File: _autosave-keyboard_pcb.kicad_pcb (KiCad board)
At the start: 2 copper layers, 436.2 x 123.8 mm, 214 parts, among them J1 Conn_01x04_Female, J2 , J3 Conn_01x03_Male, SW1 SW_Push, SW10 SW_Push, SW100 SW_Push, SW101 SW_Push, SW102 SW_Push, SW103 SW_Push, SW104 SW_Push, SW105 SW_Push, SW11 SW_Push, SW12 SW_Push, SW13 SW_Push, SW14 SW_Push, SW15 SW_Push, SW16 SW_Push, SW17 SW_Push, SW18 SW_Push, SW19 SW_Push, SW2 SW_Push, SW20 SW_Push, SW21 SW_Push, SW22 SW_Push, SW23 SW_Push, SW24 SW_Push, SW25 SW_Push, SW26 SW_Push, SW27 SW_Push, SW28 SW_Push, SW29 SW_Push, SW3 SW_Push, SW30 SW_Push, SW31 SW_Push, SW32 SW_Push, SW33 SW_Push, SW34 SW_Push, SW35 SW_Push, SW36 SW_Push, SW37 SW_Push, SW38 SW_Push, SW39 SW_Push, SW4 SW_Push, SW40 SW_Push, SW41 SW_Push, SW42 SW_Push, SW43 SW_Push, SW44 SW_Push, SW45 SW_Push, SW46 SW_Push, SW47 SW_Push, SW48 SW_Push, SW49 SW_Push, SW5 SW_Push, SW50 SW_Push, SW51 SW_Push, SW52 SW_Push, SW53 SW_Push, SW54 SW_Push, SW55 SW_Push, SW56 SW_Push, SW57 SW_Push, SW58 SW_Push, SW59 SW_Push, SW6 SW_Push, SW60 SW_Push, SW61 SW_Push, SW62 SW_Push, SW63 SW_Push, SW64 SW_Push, SW65 SW_Push, SW66 SW_Push, SW67 SW_Push, SW68 SW_Push, SW69 SW_Push, SW7 SW_Push, SW70 SW_Push, SW71 SW_Push, SW72 SW_Push, SW73 SW_Push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

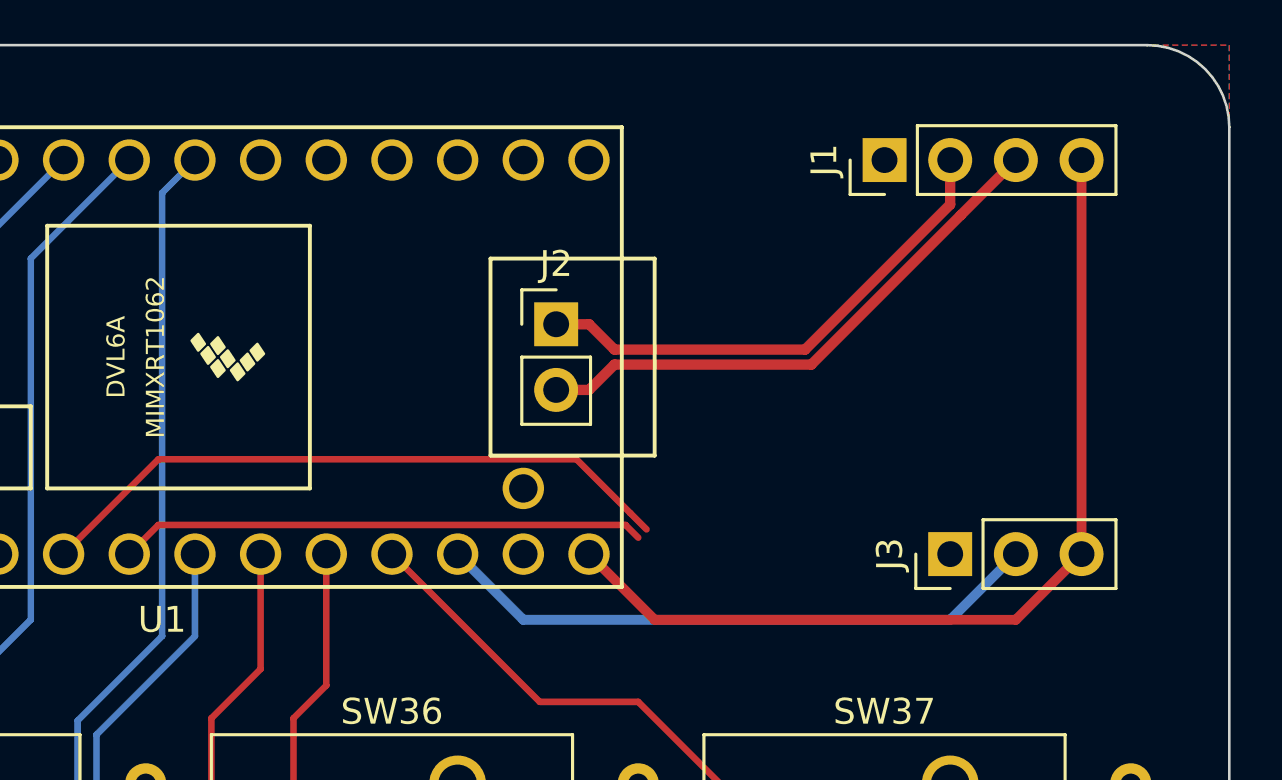
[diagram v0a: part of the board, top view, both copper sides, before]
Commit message: Add I2C port for OLED display
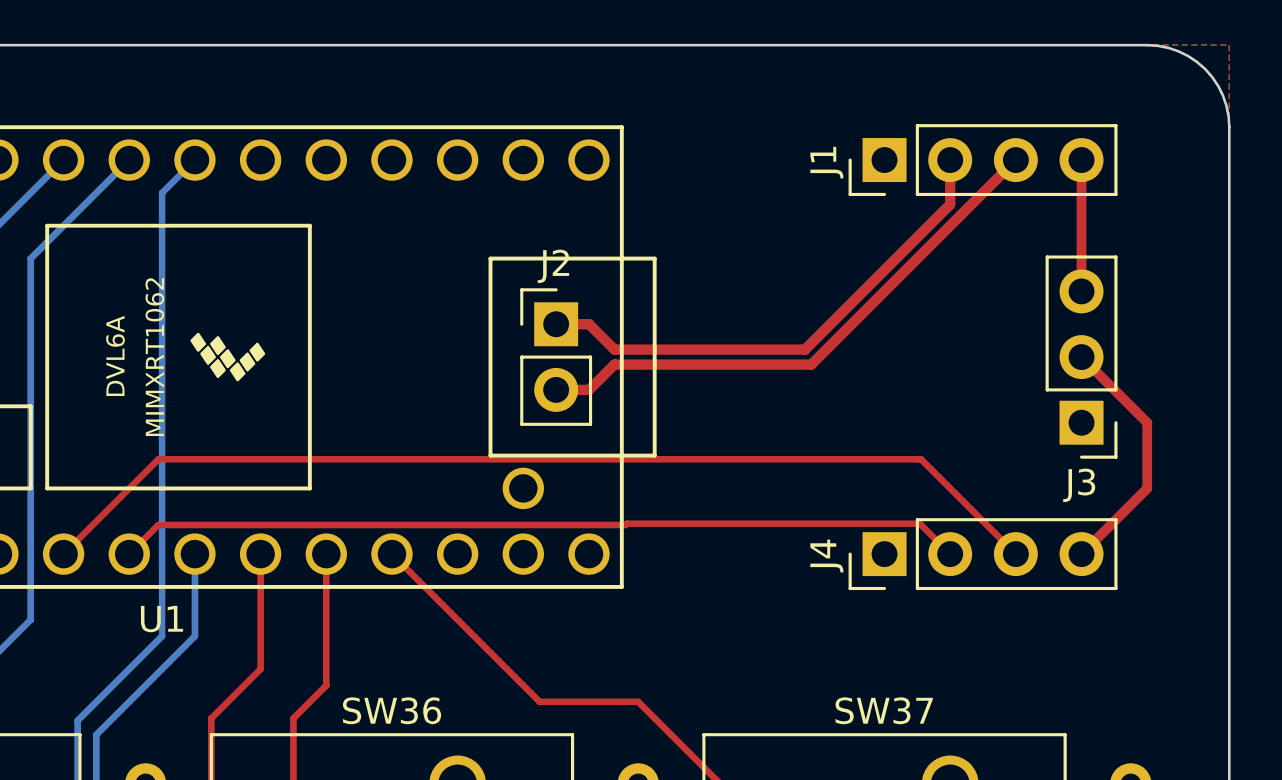
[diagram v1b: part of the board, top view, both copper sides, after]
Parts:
- added J4: Conn_01x04_Female, Connector_PinHeader_2.54mm:PinHeader_1x04_P2.54mm_Vertical, F.Cu at (407.0, 19.7)
- moved J3 7.18 mm to (414.7, 14.6), turned to 180 degrees
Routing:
- net 5V: track 36.4 -> 5.08 mm
- net SDA: track 25.2 -> 39.9 mm
- net 3V3: track 23.7 -> 9.72 mm
- net SCL: track 20.4 -> 32.7 mm
